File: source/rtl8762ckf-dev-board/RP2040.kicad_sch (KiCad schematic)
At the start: 24 parts, among them U5 RP2040, U6 W25Q16JV, U7 W25Q128JVS, Y1 12M

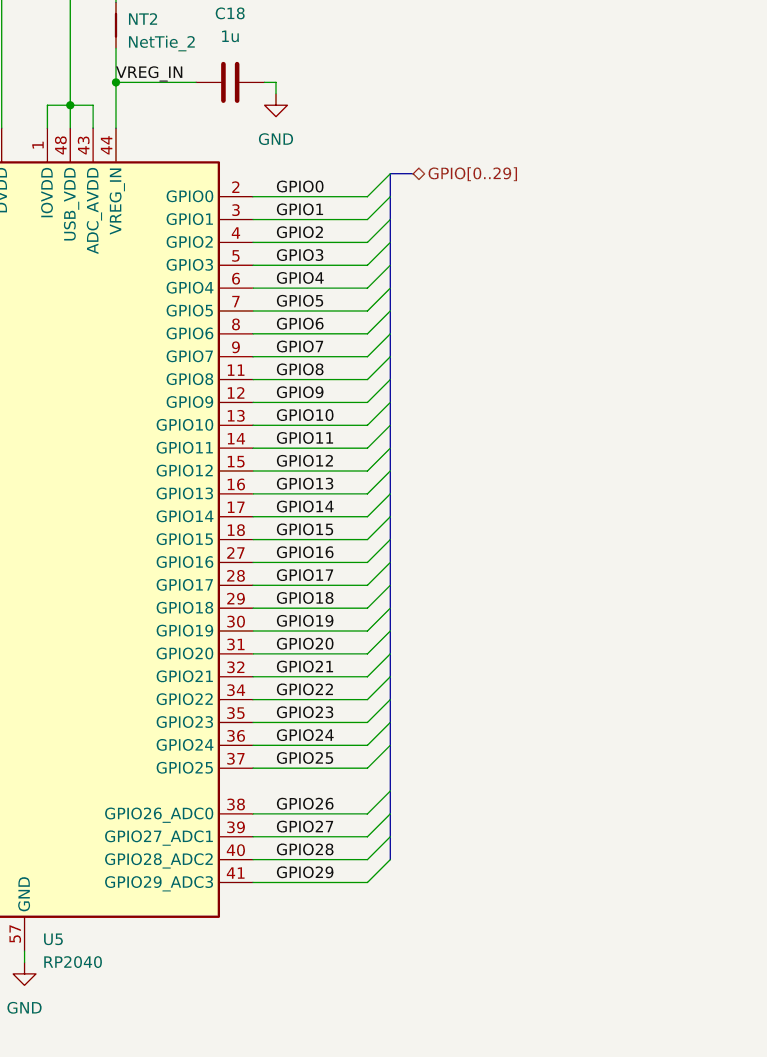
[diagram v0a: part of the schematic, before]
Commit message: add net ties to uart lines
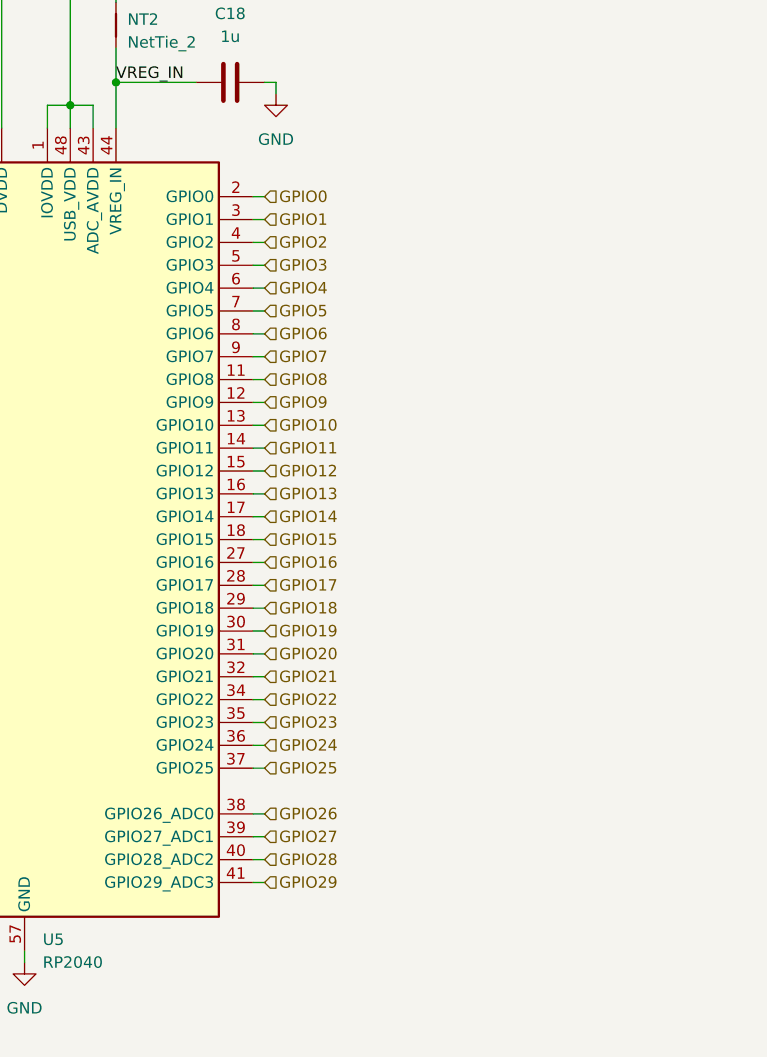
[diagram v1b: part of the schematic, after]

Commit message: set correct PNs for R5, R8, R11; closes #5
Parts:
- R14: LCSC C25086 -> C25744; MPN 0402WGF100KTCE -> 0402WGF1002TCE
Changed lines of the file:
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@@
       (effects (font (size 1.27 1.27)) hide)
     )
-    (property "LCSC" "C25086" (at 58.42 114.3 0)
+    (property "LCSC" "C25744" (at 58.42 114.3 0)
       (effects (font (size 1.27 1.27)) hide)
     )
-    (property "MPN" "0402WGF100KTCE" (at 58.42 114.3 0)
+    (property "MPN" "0402WGF1002TCE" (at 58.42 114.3 0)
       (effects (font (size 1.27 1.27)) hide)
     )
